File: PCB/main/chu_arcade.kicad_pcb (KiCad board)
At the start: 2 copper layers, 296 x 16 mm, 44 parts, among them J1 LED_In, J2 LED_Out, J3 Conn_01x04, U2 PCA9548APW, X1 GP2Y0E03_REAL, X2 GP2Y0E03_REAL, X3 GP2Y0E03_REAL, X4 GP2Y0E03_REAL, X5 GP2Y0E03_REAL, X6 GP2Y0E03_REAL

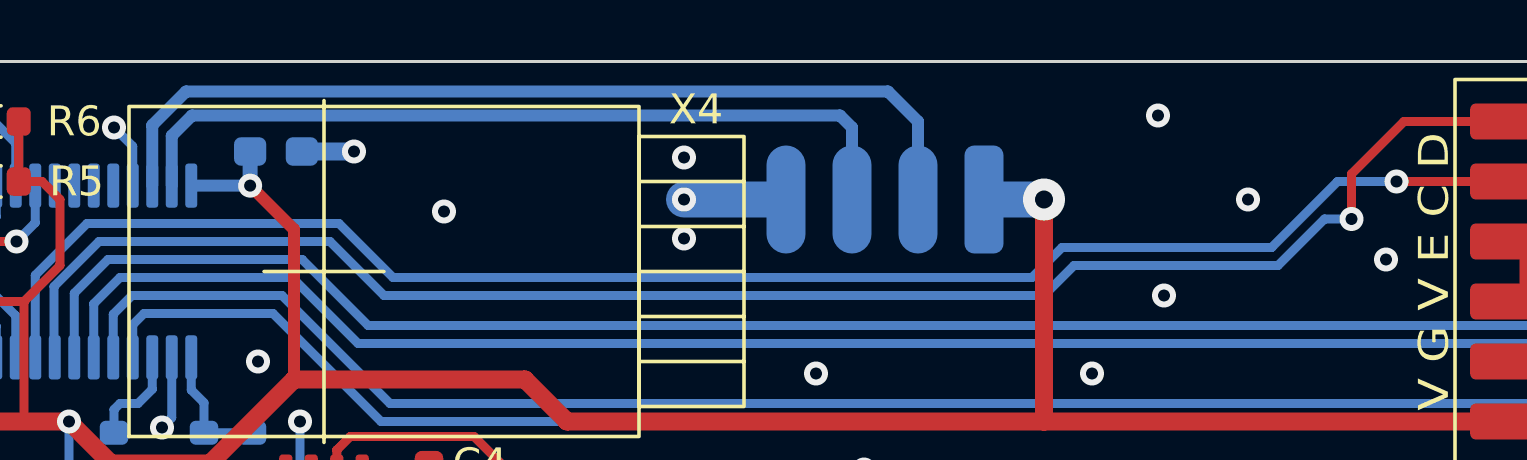
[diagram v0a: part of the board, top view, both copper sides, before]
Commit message: Add I2C main pull-up resistors
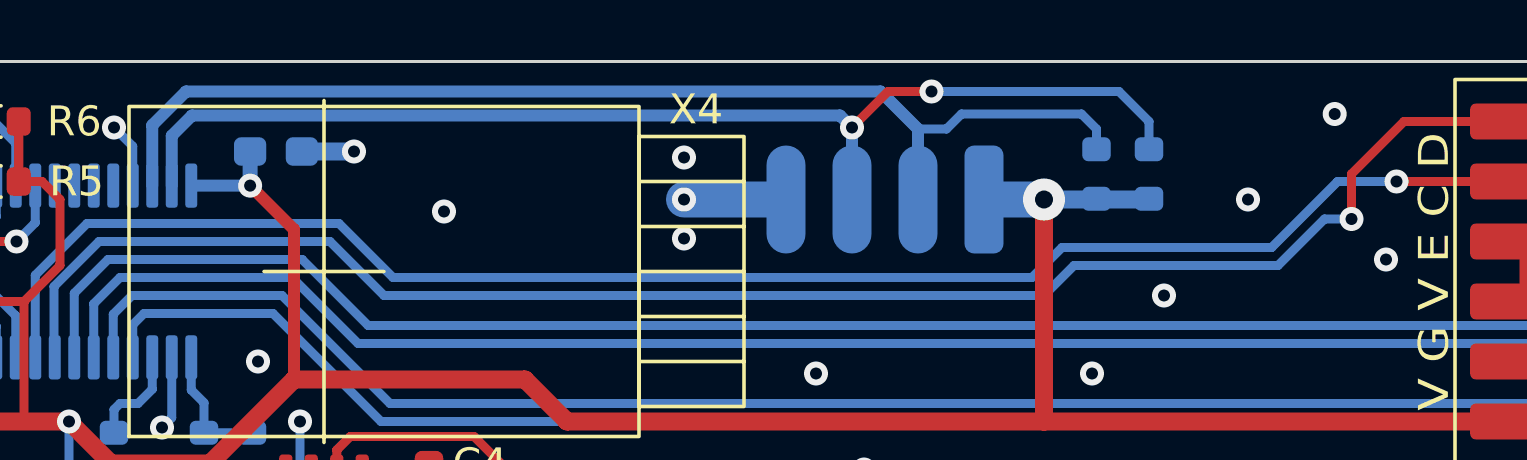
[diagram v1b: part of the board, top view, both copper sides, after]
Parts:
- added R13: 4.7K, Resistor_SMD:R_0603_1608Metric, B.Cu at (265.9, 89.8)
- added R14: 4.7K, Resistor_SMD:R_0603_1608Metric, B.Cu at (267.7, 89.8)
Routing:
- net /SDA: track 27.2 -> 38.9 mm, vias 0 -> 2
- net /SCL: track 31.2 -> 38.1 mm
- net +3V3: track 361.8 -> 365.3 mm
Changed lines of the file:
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@@
       (net 2 "+5V") (pinfunction "Pin_3") (pintype "passive"))
+  )
+  (footprint "Resistor_SMD:R_0603_1608Metric" (layer "B.Cu")
+    (at 265.946 89.824 90)
+    (descr "Resistor SMD 0603 (1608 Metric), square (rectangular) end terminal, IPC_7351 nominal, (Body size source: IPC-SM-782 page 72, https://www.pcb-3d.com/wordpress/wp-content/uploads/ipc-sm-782a_amendment_1_and_2.pdf), generated with kicad-footprint-generator")
+    (tags "resistor")
+    (property "LCSC" "C23186")
+    (property "Sheetfile" "chu_arcade.kicad_sch")
+    (property "Sheetname" "")
+    (property "ki_description" "Resistor, small symbol")
+    (property "ki_keywords" "R resistor")
+    (attr smd)
+    (fp_text reference "R13" (at 2.25 -0.75 180) (layer "B.SilkS")
+        (effects (font (size 1 1) (thickness 0.15)) (justify mirror))
+    )
+    (fp_text value "4.7K" (at 0 -1.43 90) (layer "B.Fab") hide
+        (effects (font (size 1 1) (thickness 0.15)) (justify mirror))
+    )
+    (fp_text user "${REFERENCE}" (at 0 0 90) (layer "B.Fab") hide
+        (effects (font (size 0.4 0.4) (thickness 0.06)) (justify mirror))
+    )
+    (fp_line (start -0.237258 -0.5225) (end 0.237258 -0.5225)
+      (stroke (width 0.12) (type solid)) (layer "B.SilkS"))
+    (fp_line (start -0.237258 0.5225) (end 0.237258 0.5225)
+      (stroke (width 0.12) (type solid)) (layer "B.SilkS"))
+    (fp_line (start -1.48 -0.73) (end -1.48 0.73)
+      (stroke (width 0.05) (type solid)) (layer "B.CrtYd"))
+    (fp_line (start -1.48 0.73) (end 1.48 0.73)
+      (stroke (width 0.05) (type solid)) (layer "B.CrtYd"))
+    (fp_line (start 1.48 -0.73) (end -1.48 -0.73)
+      (stroke (width 0.05) (type solid)) (layer "B.CrtYd"))
+    (fp_line (start 1.48 0.73) (end 1.48 -0.73)
+      (stroke (width 0.05) (type solid)) (layer "B.CrtYd"))
+    (fp_line (start -0.8 -0.4125) (end -0.8 0.4125)
+      (stroke (width 0.1) (type solid)) (layer "B.Fab"))
+    (fp_line (start -0.8 0.4125) (end 0.8 0.4125)
+      (stroke (width 0.1) (type solid)) (layer "B.Fab"))
+    (fp_line (start 0.8 -0.4125) (end -0.8 -0.4125)
+      (stroke (width 0.1) (type solid)) (layer "B.Fab"))
+    (fp_line (start 0.8 0.4125) (end 0.8 -0.4125)
+      (stroke (width 0.1) (type solid)) (layer "B.Fab"))
+    (pad "1" smd roundrect (at -0.825 0 90) (size 0.8 0.95) (layers "B.Cu" "B.Paste" "B.Mask") (roundrect_rratio 0.25)
+      (net 3 "+3V3") (pintype "passive"))
+    (pad "2" smd roundrect (at 0.825 0 90) (size 0.8 0.95) (layers "B.Cu" "B.Paste" "B.Mask") (roundrect_rratio 0.25)
+      (net 4 "/SCL") (pintype "passive"))
+    (model "${KICAD6_3DMODEL_DIR}/Resistor_SMD.3dshapes/R_0603_1608Metric.wrl"
+      (offset (xyz 0 0 0))
+      (scale (xyz 1 1 1))
+      (rotate (xyz 0 0 0))
+    )
   )
   (footprint "chu_arcade:Solder_3P" (layer "B.Cu")
@@
     (pad "3" smd oval (at 0 -2.2 180) (size 3.6 1.3) (layers "B.Cu" "B.Paste" "B.Mask")
       (net 2 "+5V") (pinfunction "Pin_3") (pintype "passive"))
+  )
+  (footprint "Resistor_SMD:R_0603_1608Metric" (layer "B.Cu")
+    (at 267.696 89.824 90)
+    (descr "Resistor SMD 0603 (1608 Metric), square (rectangular) end terminal, IPC_7351 nominal, (Body size source: IPC-SM-782 page 72, https://www.pcb-3d.com/wordpress/wp-content/uploads/ipc-sm-782a_amendment_1_and_2.pdf), generated with kicad-footprint-generator")
+    (tags "resistor")
+    (property "LCSC" "C23186")
+    (property "Sheetfile" "chu_arcade.kicad_sch")
+    (property "Sheetname" "")
+    (property "ki_description" "Resistor, small symbol")
+    (property "ki_keywords" "R resistor")
+    (attr smd)
+    (fp_text reference "R14" (at 2.25 0.75 180) (layer "B.SilkS")
+        (effects (font (size 1 1) (thickness 0.15)) (justify mirror))
+    )
+    (fp_text value "4.7K" (at 0 -1.43 90) (layer "B.Fab") hide
+        (effects (font (size 1 1) (thickness 0.15)) (justify mirror))
+    )
+    (fp_text user "${REFERENCE}" (at -0.35 -1.58 90) (layer "B.Fab") hide
+        (effects (font (size 0.4 0.4) (thickness 0.06)) (justify mirror))
+    )
+    (fp_line (start -0.237258 -0.5225) (end 0.237258 -0.5225)
+      (stroke (width 0.12) (type solid)) (layer "B.SilkS"))
+    (fp_line (start -0.237258 0.5225) (end 0.237258 0.5225)
+      (stroke (width 0.12) (type solid)) (layer "B.SilkS"))
+    (fp_line (start -1.48 -0.73) (end -1.48 0.73)
+      (stroke (width 0.05) (type solid)) (layer "B.CrtYd"))
+    (fp_line (start -1.48 0.73) (end 1.48 0.73)
+      (stroke (width 0.05) (type solid)) (layer "B.CrtYd"))
+    (fp_line (start 1.48 -0.73) (end -1.48 -0.73)
+      (stroke (width 0.05) (type solid)) (layer "B.CrtYd"))
+    (fp_line (start 1.48 0.73) (end 1.48 -0.73)
+      (stroke (width 0.05) (type solid)) (layer "B.CrtYd"))
+    (fp_line (start -0.8 -0.4125) (end -0.8 0.4125)
+      (stroke (width 0.1) (type solid)) (layer "B.Fab"))
+    (fp_line (start -0.8 0.4125) (end 0.8 0.4125)
+      (stroke (width 0.1) (type solid)) (layer "B.Fab"))
+    (fp_line (start 0.8 -0.4125) (end -0.8 -0.4125)
+      (stroke (width 0.1) (type solid)) (layer "B.Fab"))
+    (fp_line (start 0.8 0.4125) (end 0.8 -0.4125)
+      (stroke (width 0.1) (type solid)) (layer "B.Fab"))
+    (pad "1" smd roundrect (at -0.825 0 90) (size 0.8 0.95) (layers "B.Cu" "B.Paste" "B.Mask") (roundrect_rratio 0.25)
+      (net 3 "+3V3") (pintype "passive"))
+    (pad "2" smd roundrect (at 0.825 0 90) (size 0.8 0.95) (layers "B.Cu" "B.Paste" "B.Mask") (roundrect_rratio 0.25)
+      (net 5 "/SDA") (pintype "passive"))
+    (model "${KICAD6_3DMODEL_DIR}/Resistor_SMD.3dshapes/R_0603_1608Metric.wrl"
+      (offset (xyz 0 0 0))
+      (scale (xyz 1 1 1))
+      (rotate (xyz 0 0 0))
+    )
   )
   (footprint "Resistor_SMD:R_0603_1608Metric" (layer "B.Cu")
@@
   (via (at 68.396 89.074) (size 0.8) (drill 0.4) (layers "F.Cu" "B.Cu") (free) (net 1))
   (via (at 178.596 96.674) (size 0.8) (drill 0.4) (layers "F.Cu" "B.Cu") (free) (net 1))
-  (via (at 267.996 87.874) (size 0.8) (drill 0.4) (layers "F.Cu" "B.Cu") (free) (net 1))
+  (via (at 273.886 87.824) (size 0.8) (drill 0.4) (layers "F.Cu" "B.Cu") (free) (net 1))
   (via (at 233.196 88.274) (size 0.8) (drill 0.4) (layers "F.Cu" "B.Cu") (free) (net 1))
   (via (at 265.796 96.474) (size 0.8) (drill 0.4) (layers "F.Cu" "B.Cu") (free) (net 1))
@@
   (via (at 237.7335 90.2115) (size 0.8) (drill 0.4) (layers "F.Cu" "B.Cu") (net 3))
   (via (at 231.696 98.074) (size 0.8) (drill 0.4) (layers "F.Cu" "B.Cu") (net 3))
+  (segment (start 264.196 90.674) (end 267.671 90.674) (width 0.6) (layer "B.Cu") (net 3))
   (segment (start 264.196 90.674) (end 262.196 90.674) (width 1.2) (layer "B.Cu") (net 3))
   (segment (start 232.021 100.099) (end 236.196 100.099) (width 0.3) (layer "B.Cu") (net 3))
@@
   (segment (start 237.7335 90.2115) (end 235.796 90.2115) (width 0.4) (layer "B.Cu") (net 3))
   (segment (start 237.7335 90.2115) (end 237.7335 89.074) (width 0.5) (layer "B.Cu") (net 3))
-  (segment (start 259.996 88.074) (end 258.996 87.074) (width 0.4) (layer "B.Cu") (net 4))
   (segment (start 235.596 87.074) (end 234.471 88.199) (width 0.4) (layer "B.Cu") (net 4))
-  (segment (start 259.996 90.874) (end 259.996 88.074) (width 0.4) (layer "B.Cu") (net 4))
+  (segment (start 258.746 87.074) (end 235.596 87.074) (width 0.4) (layer "B.Cu") (net 4))
+  (segment (start 259.996 88.324) (end 258.746 87.074) (width 0.4) (layer "B.Cu") (net 4))
+  (segment (start 259.996 90.874) (end 259.996 88.324) (width 0.4) (layer "B.Cu") (net 4))
+  (segment (start 259.996 88.324) (end 260.946 88.324) (width 0.3) (layer "B.Cu") (net 4))
+  (segment (start 265.946 88.324) (end 265.946 88.999) (width 0.3) (layer "B.Cu") (net 4))
   (segment (start 234.471 88.199) (end 234.471 90.2115) (width 0.4) (layer "B.Cu") (net 4))
-  (segment (start 258.996 87.074) (end 235.596 87.074) (width 0.4) (layer "B.Cu") (net 4))
+  (segment (start 261.446 87.824) (end 265.446 87.824) (width 0.3) (layer "B.Cu") (net 4))
+  (segment (start 265.446 87.824) (end 265.946 88.324) (width 0.3) (layer "B.Cu") (net 4))
+  (segment (start 260.946 88.324) (end 261.446 87.824) (width 0.3) (layer "B.Cu") (net 4))
+  (segment (start 258.996 87.074) (end 257.796 88.274) (width 0.3) (layer "F.Cu") (net 5))
+  (segment (start 260.446 87.074) (end 258.996 87.074) (width 0.3) (layer "F.Cu") (net 5))
+  (via (at 257.796 88.274) (size 0.8) (drill 0.4) (layers "F.Cu" "B.Cu") (net 5))
+  (via (at 260.446 87.074) (size 0.8) (drill 0.4) (layers "F.Cu" "B.Cu") (net 5))
+  (segment (start 267.696 88.074) (end 267.696 88.999) (width 0.3) (layer "B.Cu") (net 5))
+  (segment (start 266.696 87.074) (end 267.696 88.074) (width 0.3) (layer "B.Cu") (net 5))
   (segment (start 257.796 88.274) (end 257.796 90.674) (width 0.4) (layer "B.Cu") (net 5))
   (segment (start 235.121 88.549) (end 235.796 87.874) (width 0.4) (layer "B.Cu") (net 5))
+  (segment (start 260.446 87.074) (end 266.696 87.074) (width 0.3) (layer "B.Cu") (net 5))
   (segment (start 235.796 87.874) (end 257.396 87.874) (width 0.4) (layer "B.Cu") (net 5))
   (segment (start 257.396 87.874) (end 257.796 88.274) (width 0.4) (layer "B.Cu") (net 5))
